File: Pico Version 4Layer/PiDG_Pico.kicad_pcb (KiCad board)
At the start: 4 copper layers, 126 x 126 mm, 86 parts, among them J1 Conn_02x05_Odd_Even, J10 Trig, J11 Laser Enable, J12 Pixel Reset, J14 Pico Socket A, J15 Pico Socket B, J16 Laser En/PWM Trig/GND, J17 USB-C PD in, J18 Laser 1 mode, J19 Laser 2 mode, J2 Conn_02x05_Odd_Even, J3 Conn_02x05_Odd_Even, J4 Conn_02x05_Odd_Even, J5 Conn_02x05_Odd_Even, J6 Conn_02x05_Odd_Even, J7 Laser 1, J8 Laser 2, U1 74LVC1G04, U10 74AHCT1G08, U12 74LVC1G17, U13 UCC27524, U14 CH224K, U15 AP63205WU, U16 LM66100, U17 LT3065EDD, U18 TPS3700DDC, U2 SN74LVC04AD, U3 74LVC1G00, U4 SN74LVC04AD, U5 74LVC1G04, U6 SN74LVC04AD, U7 74AHCT1G08, U8 74AHCT1G08, U9 NCP718xSN180

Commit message: Update Pico hardware and fabrication files
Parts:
- R11: value 1k -> 0
- R15: value 10k -> 0
- U14: value CH224K -> CH224A
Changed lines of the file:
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@@
 			)
 		)
-		(property "Description" "CH224K CFG1: 56k to GND requests 15 V (6k8=9 V, 24k=12 V, open=20 V)"
+		(property "Description" "CH224A CFG1: 56k to GND requests 15 V (6k8=9 V, 24k=12 V, 120k=20 V, 210k=28 V; open is outside the table)"
 			(at 0 0 270)
 			(layer "F.Fab")
@@
 			)
 		)
-		(property "Value" "10k"
+		(property "Value" "0"
 			(at 0 1.65 90)
 			(layer "F.Fab")
@@
 			)
 		)
-		(property "Description" "CH224K VBUS sense resistor (datasheet: 10k)"
+		(property "Description" "CH224A VBUS (pin 8) shorted to VHV: 0 ohm, per WCH guide 7.2.1 (was 10k for CH224K)"
 			(at 0 0 90)
 			(layer "F.Fab")
@@
 			)
 		)
-		(property "Description" "CH224K VDD decoupling"
+		(property "Description" "CH224A VHV decoupling (on VBUS_PD, up to 20 V)"
 			(at 0 0 180)
 			(layer "F.Fab")
@@
 			)
 		)
-		(property "Value" "1k"
+		(property "Value" "0"
 			(at 0 1.83 90)
 			(layer "F.Fab")
@@
 			)
 		)
-		(property "Description" "CH224K VDD feed (datasheet: 1k). 1206: dissipates 0.14 W at 15 V"
+		(property "Description" "CH224A VHV (pin 1) feed: 0 ohm, per WCH CH224K-to-CH224A guide 7.2.1 (was 1k for CH224K VDD)"
 			(at 0 0 90)
 			(layer "F.Fab")
@@
 			)
 		)
-		(property "Value" "CH224K"
+		(property "Value" "CH224A"
 			(at 0 3.4 270)
 			(layer "F.Fab")
@@
 			)
 		)
-		(property "Description" "USB PD sink controller. R10 = 56k on CFG1 requests 15 V."
+		(property "Description" "USB PD sink controller, WCH CH224A (pin-compatible successor of the discontinued CH224K). R10 = 56k on CFG1 requests 15 V."
 			(at 0 0 270)
 			(layer "F.Fab")

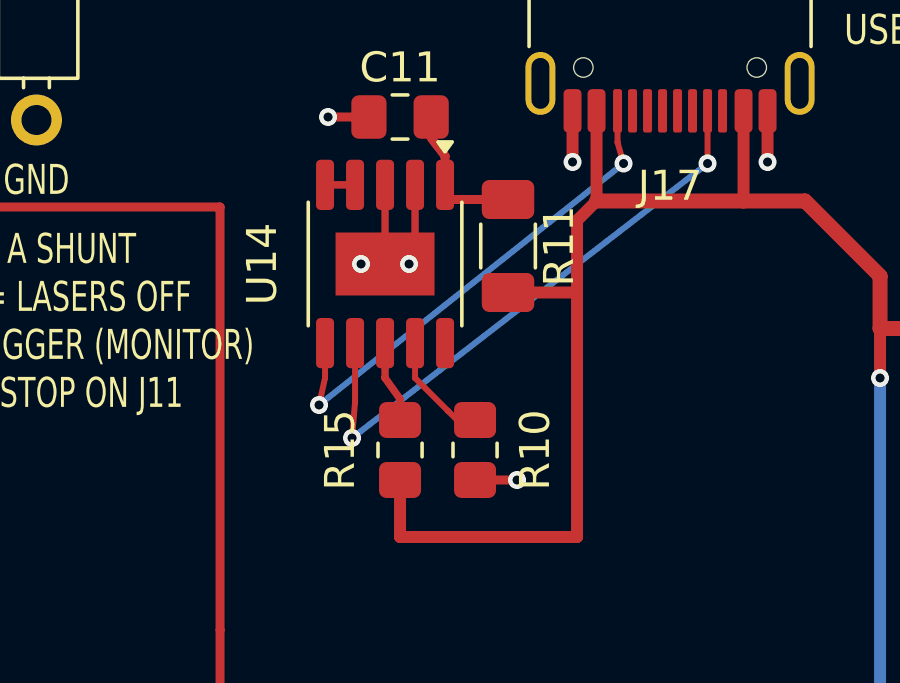
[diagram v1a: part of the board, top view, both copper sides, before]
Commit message: Remove CH224A jumpers and update fabrication files
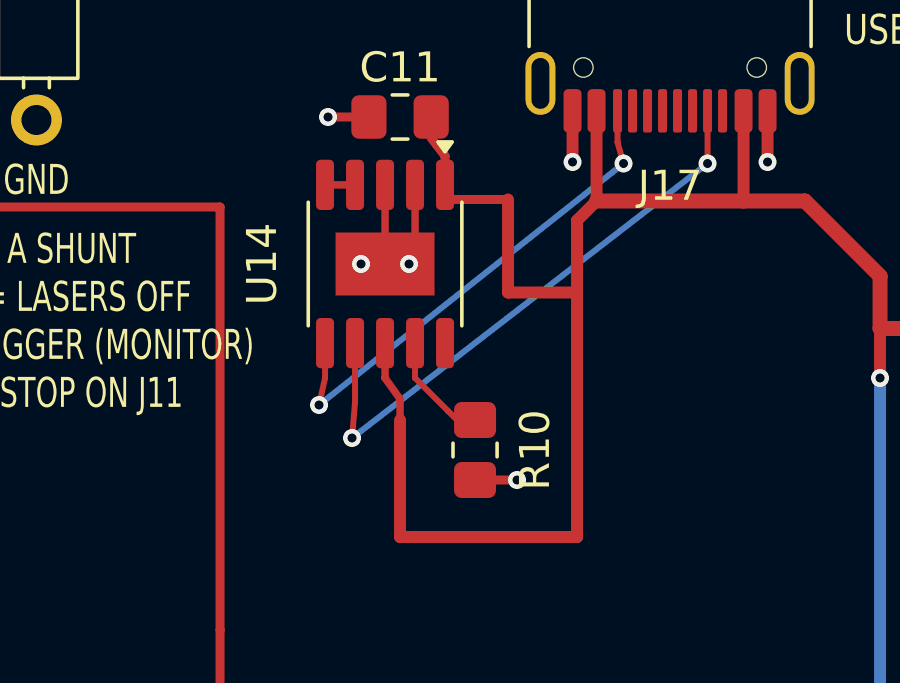
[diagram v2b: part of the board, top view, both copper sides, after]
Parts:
- removed R11: 0, Resistor_SMD:R_1206_3216Metric_Pad1.30x1.75mm_HandSolder
- removed R15: 0, Resistor_SMD:R_0805_2012Metric_Pad1.20x1.40mm_HandSolder
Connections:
- C11 pad 1: Net-(U14-VDD) -> VBUS_PD
- U14 pad 1: Net-(U14-VDD) -> VBUS_PD
- U14 pad 8: Net-(U14-VBUS) -> VBUS_PD
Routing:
- net VBUS_PD: track 95.1 -> 107.2 mm
- net Net-(U14-VDD): track 4.31 -> 0.00 mm
- net Net-(U14-VBUS): track 2.72 -> 0.00 mm
